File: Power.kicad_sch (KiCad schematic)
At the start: 57 parts, among them J6 Conn_01x02, Q3 AON7534, Q4 AON7534, U10 MAX17320G22+, U5 TPS259474ARPWR, U6 TPS2116DRL, U7 TPS61033DRLR, U9 BQ25798

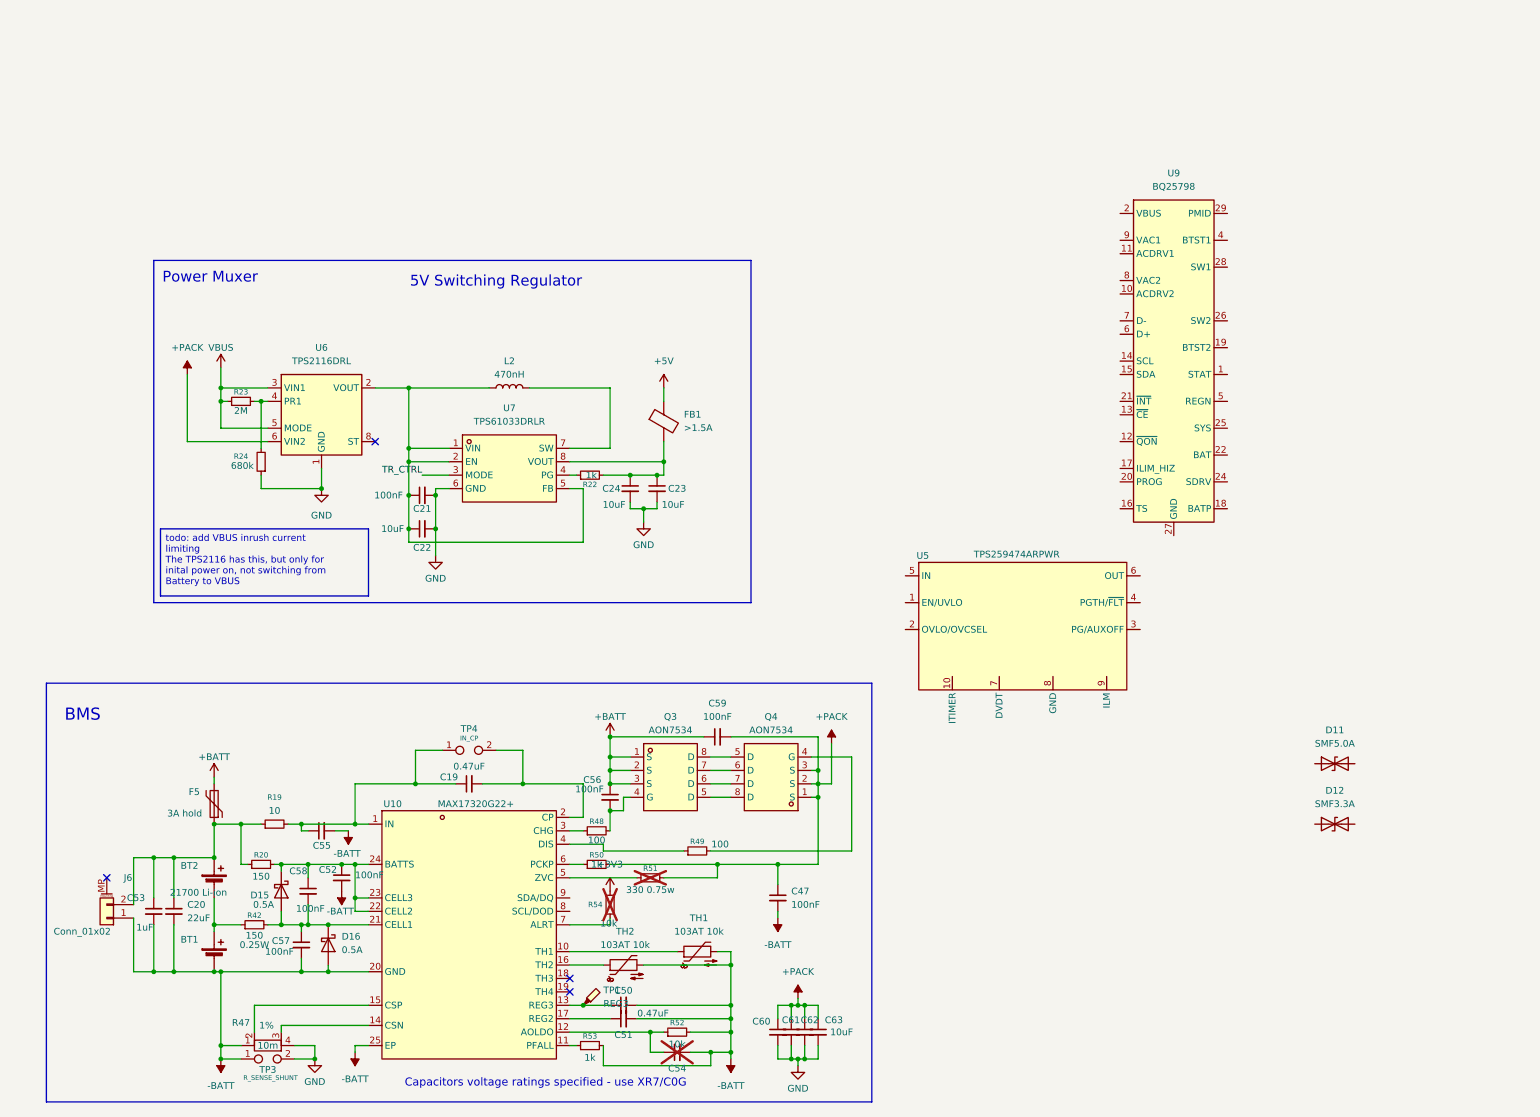
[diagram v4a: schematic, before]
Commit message: wired BQ25798 schematic
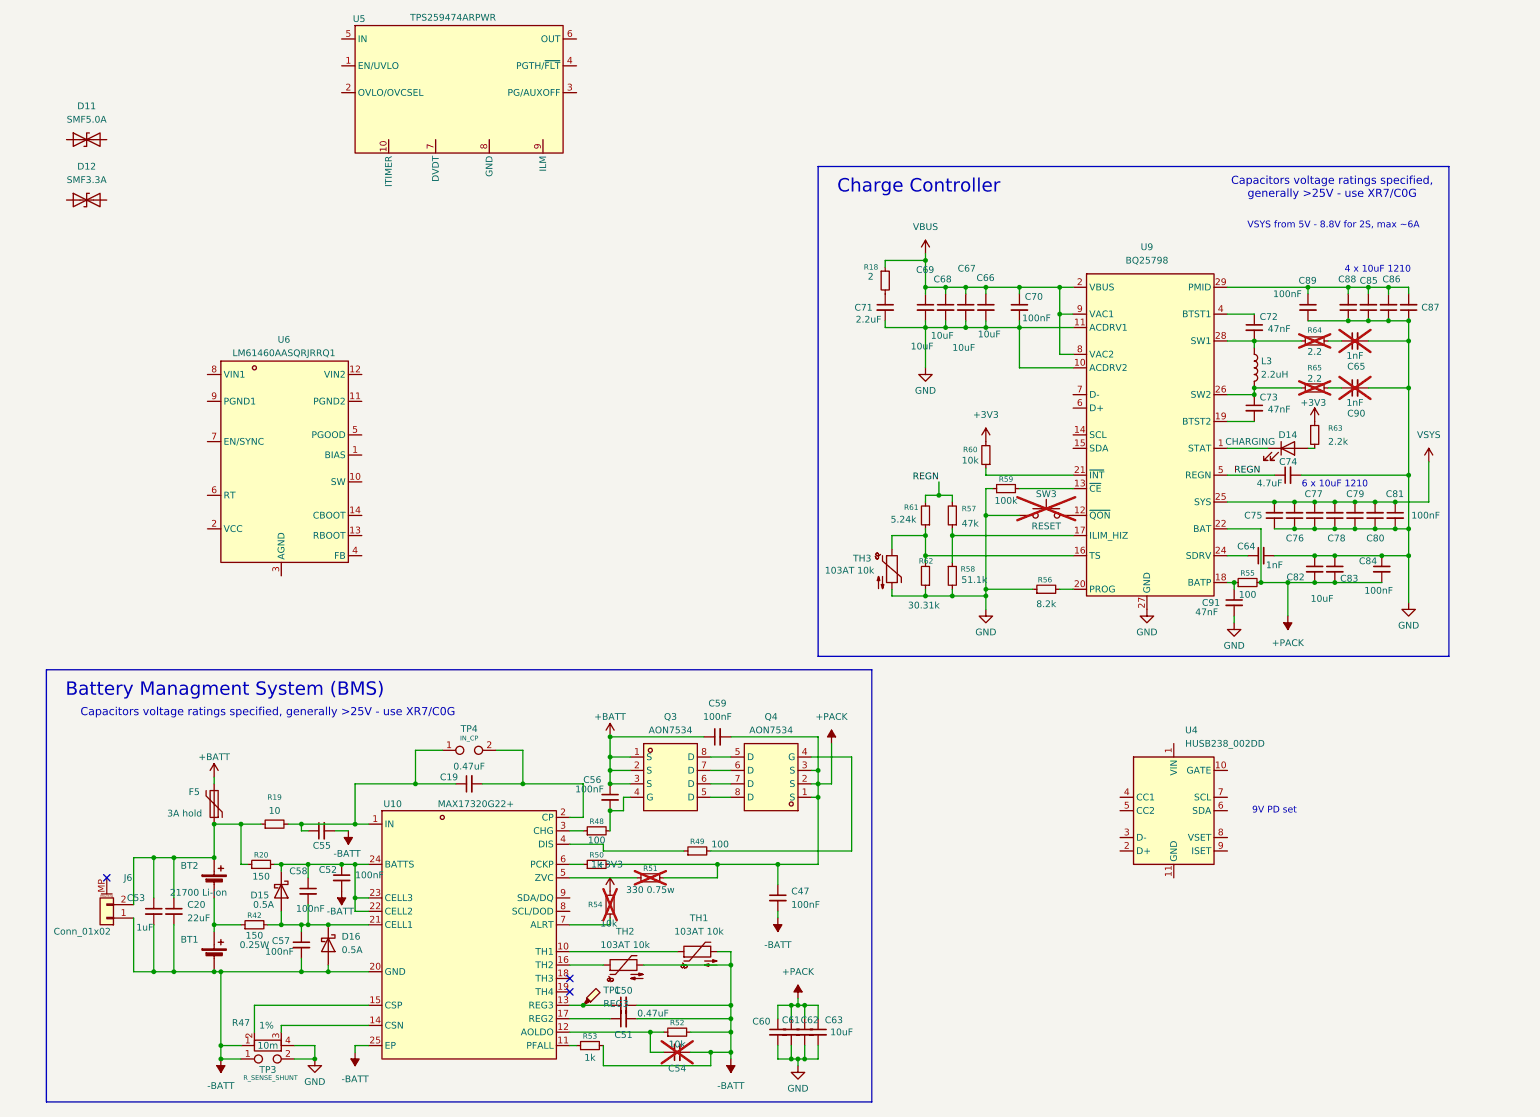
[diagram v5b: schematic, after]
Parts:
- removed C21: 100nF, Capacitor_SMD:C_0402_1005Metric, symbol Device:C_Small
- removed C22, C23, C24: 10uF, Capacitor_SMD:C_0402_1005Metric, symbol Device:C_Small
- removed FB1: >1.5A, Inductor_SMD:L_0805_2012Metric_Pad1.05x1.20mm_HandSolder, symbol Device:FerriteBead
- removed L2: 470nH, Inductor_SMD:L_1008_2520Metric_Pad1.43x2.20mm_HandSolder, symbol Device:L
- removed R22: 1k, Resistor_SMD:R_0402_1005Metric, symbol Device:R_Small
- removed R23: 2M, Resistor_SMD:R_0402_1005Metric, symbol Device:R_Small
- removed R24: 680k, Resistor_SMD:R_0402_1005Metric, symbol Device:R_Small
- removed U6: TPS2116DRL, Package_TO_SOT_SMD:SOT-583-8, symbol Power_Management:TPS2116DRL
- removed U7: TPS61033DRLR, Package_TO_SOT_SMD:SOT-583-8, symbol easyeda2kicad:TPS61033DRLR
- added C64: 1nF, Capacitor_SMD:C_0402_1005Metric, symbol Device:C_Small
- added C65, C90: 1nF, Capacitor_SMD:C_0402_1005Metric_Pad0.74x0.62mm_HandSolder, symbol Device:C_Small
- added C66, C67, C68, C69, C75, C76, C77, C78, C79, C80, C82, C83, C85, C86, C87, C88: 10uF, Capacitor_SMD:C_1210_3225Metric, symbol Device:C_Small
- added C70, C81, C84, C89: 100nF, Capacitor_SMD:C_0402_1005Metric, symbol Device:C_Small
- added C71: 2.2uF, Capacitor_SMD:C_0805_2012Metric, symbol Device:C_Small
- added C72, C73, C91: 47nF, Capacitor_SMD:C_0402_1005Metric, symbol Device:C_Small
- added C74: 4.7uF, Capacitor_SMD:C_0603_1608Metric, symbol Device:C_Small
- added D14: CHARGING, symbol Device:LED
- added L3: 2.2uH, symbol Device:L
- added R18: 2, Resistor_SMD:R_0402_1005Metric, symbol Device:R_Small
- added R55: 100, Resistor_SMD:R_0402_1005Metric, symbol Device:R_Small
- added R56: 8.2k, Resistor_SMD:R_0402_1005Metric_Pad0.72x0.64mm_HandSolder, symbol Device:R_Small
- added R57: 47k, Resistor_SMD:R_0603_1608Metric_Pad0.98x0.95mm_HandSolder, symbol Device:R_Small
- added R58: 51.1k, Resistor_SMD:R_0603_1608Metric_Pad0.98x0.95mm_HandSolder, symbol Device:R_Small
- added R59: 100k, Resistor_SMD:R_0402_1005Metric, symbol Device:R_Small
- added R60: 10k, Resistor_SMD:R_0402_1005Metric, symbol Device:R_Small
- added R61: 5.24k, Resistor_SMD:R_0603_1608Metric_Pad0.98x0.95mm_HandSolder, symbol Device:R_Small
- added R62: 30.31k, Resistor_SMD:R_0603_1608Metric_Pad0.98x0.95mm_HandSolder, symbol Device:R_Small
- added R63: 2.2k, Resistor_SMD:R_0402_1005Metric_Pad0.72x0.64mm_HandSolder, symbol Device:R_Small
- added R64, R65: 2.2, Resistor_SMD:R_0402_1005Metric_Pad0.72x0.64mm_HandSolder, symbol Device:R_Small
- added SW3: RESET, symbol Switch:SW_Push
- added TH3: 103AT 10k, symbol Device:Thermistor_NTC
- added U4: HUSB238_002DD, Package_DFN_QFN:WDFN-10-1EP_3x3mm_P0.5mm_EP1.8x2.5mm, symbol Interface_USB:HUSB238_xxxDD
- added U6: LM61460AASQRJRRQ1, easyeda2kicad:VQFN-14-HR_L4.0-W3.5-TL_LM61460AASQRJRRQ1, symbol easyeda2kicad:LM61460AASQRJRRQ1
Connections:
- net +3V3: now also R60.2, R63.1
- net +PACK: now also U9.22 (BAT), U9.23 (BAT), C82.2, C83.2, C84.2, R55.2
- net GND: now also U9.10 (ACDRV2), U9.11 (ACDRV1), U9.27 (GND), C64.2, C65.2, C66.2, C67.2, C68.2, C69.2, C70.2, C71.2, C74.2, C75.1, C76.1, C77.1, C78.1, C79.1, C80.1, C81.2, C82.1, C83.1, C84.1, C85.1, C86.1, C87.1, C88.1, C89.2, C90.2, C91.2, R56.1, R58.2, R59.1, R62.1, SW3.1, TH3.2
- net VBUS: now also U9.2 (VBUS), U9.3 (VBUS), U9.8 (VAC2), U9.9 (VAC1), C66.1, C67.1, C68.1, C69.1, C70.1, R18.1
- net at U9.1 (STAT): now also D14.1 (K)
- net at U9.12 (~{QON}): now also SW3.2
- net at U9.13 (~{CE}): now also R59.2
- net at U9.16 (TS): now also R61.1, R62.2, TH3.1
- net at U9.17 (ILIM_HIZ): now also R57.1, R58.1
- net at U9.18 (BATP): now also C91.1, R55.1
- net at U9.19 (BTST2): now also C73.2
- net at U9.20 (PROG): now also R56.2
- net at U9.21 (~{INT}): now also R60.1
- net at U9.24 (SDRV): now also C64.1
- net VSYS: now reaches U9.25 (SYS)
- net VSYS: now also C75.2, C76.2, C77.2, C78.2, C79.2, C80.2, C81.1
- net at U9.26 (SW2): now also C73.1, L3.2, R65.1
- net at U9.28 (SW1): now also C72.2, L3.1, R64.1
- net at U9.29 (PMID): now also C85.2, C86.2, C87.2, C88.2, C89.1
- net at U9.4 (BTST1): now also C72.1
- net REGN: now reaches U9.5 (REGN)
- net REGN: now also C74.1, R57.2, R61.2
- new net: C71.1, R18.2
- new net: C90.1, R65.2
- new net: C65.1, R64.2
- new net: D14.2 (A), R63.2
- no-connect marks 4 -> 3
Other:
- note added: "4 x 10uF 1210"
- note added: "6 x 10uF 1210"
- note added: "9V PD set"
- note added: "Battery Managment System (BMS)"
- note added: "Capacitors voltage ratings specified, generally >25V - use XR7/C0G"
- note added: "Charge Controller"
- note added: "VSYS from 5V - 8.8V for 2S, max ~6A"
- note removed: "5V Switching Regulator"
- note removed: "BMS"
- note removed: "Capacitors voltage ratings specified - use XR7/C0G"
- note removed: "Power Muxer"
- moved on the sheet: D11, D12, U5, U9

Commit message: changes
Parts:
- added C100, C103, C97: 100nF, Capacitor_SMD:C_0402_1005Metric, symbol Device:C_Small
- added C101, C94, C95, C98, C99: 10uF, Capacitor_SMD:C_1210_3225Metric, symbol Device:C_Small
- added C102, C96: 1uF, Capacitor_SMD:C_0603_1608Metric, symbol Device:C_Small
- added C104, C105: 2.2uF, Capacitor_SMD:C_0603_1608Metric, symbol Device:C_Small
- added C106: 22pF C0G, Capacitor_SMD:C_0402_1005Metric_Pad0.74x0.62mm_HandSolder, symbol Device:C_Small
- added C107, C92: 1uF, Capacitor_SMD:C_0402_1005Metric, symbol Device:C_Small
- added C109, C110: 2.2uF, symbol Device:C_Small
- added C21, C23, C24: 22uF, Capacitor_SMD:C_1206_3216Metric, symbol Device:C_Small
- added C22: 1nF, Capacitor_SMD:C_0402_1005Metric_Pad0.74x0.62mm_HandSolder, symbol Device:C_Small
- added JP9: SolderJumper_3_Bridged12, Jumper:SolderJumper-3_P1.3mm_Bridged12_RoundedPad1.0x1.5mm_NumberLabels, symbol Jumper:SolderJumper_3_Bridged12
- added L2: 1.5uH, symbol Device:L
- added R22: 6.04k, Resistor_SMD:R_0402_1005Metric_Pad0.72x0.64mm_HandSolder, symbol Device:R_Small
- added R23: 100k, Resistor_SMD:R_0402_1005Metric, symbol Device:R_Small
- added R24: 24.3k, Resistor_SMD:R_0402_1005Metric_Pad0.72x0.64mm_HandSolder, symbol Device:R_Small
- added R66: 100, Resistor_SMD:R_0402_1005Metric_Pad0.72x0.64mm_HandSolder, symbol Device:R_Small
- added R67: 10, Resistor_SMD:R_0402_1005Metric, symbol Device:R_Small
- added R68, R71: 100k, symbol Device:R_Small
- added R69: 1k, Resistor_SMD:R_0402_1005Metric_Pad0.72x0.64mm_HandSolder, symbol Device:R_Small
- added R70: 402k, symbol Device:R_Small
- added R72: 2.2, Resistor_SMD:R_0402_1005Metric_Pad0.72x0.64mm_HandSolder, symbol Device:R_Small
- added TP5: 5V, TestPoint:TestPoint_2Pads_Pitch2.54mm_Drill0.8mm, symbol Connector:TestPoint_2Pole
- added TP6: VSYS, TestPoint:TestPoint_2Pads_Pitch2.54mm_Drill0.8mm, symbol Connector:TestPoint_2Pole
- added TP8: PGOOD, TestPoint:TestPoint_Loop_D2.54mm_Drill1.5mm_Beaded, symbol Connector:TestPoint_Probe
- added U12: AP2112K-3.3TRG1, Package_TO_SOT_SMD:SOT-23-5, symbol Regulator_Linear:AP2112K-3.3
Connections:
- net +3V3: now also C107.1, C110.1, R68.1, U12.5 (VOUT)
- net GND: now also U6.11 (PGND2), U6.3 (AGND), U6.9 (PGND1), C100.1, C101.2, C102.2, C104.2, C105.1, C107.2, C109.2, C110.2, C21.2, C22.2, C23.2, C24.1, C92.2, C94.1, C95.1, C96.1, C97.2, C98.2, C99.2, R22.1, R24.1, R71.2, TP5.1, TP6.2, U12.2 (GND)
- net VSYS: now also U6.12 (VIN2), U6.8 (VIN1), C100.2, C101.1, C102.1, C94.2, C95.2, C96.2, C97.1, C98.1, C99.1, R70.1, TP6.1
- net at U6.1 (BIAS): now also C105.2, R67.1
- net at U6.10 (SW): now also C103.1, L2.1, R72.1
- net at U6.13 (RBOOT): now also R66.2
- net at U6.14 (CBOOT): now also C103.2, R66.1
- net at U6.2 (VCC): now also C104.1
- net at U6.4 (FB): now also C106.2, R23.1, R24.2
- net PGOOD: now reaches U6.5 (PGOOD)
- net PGOOD: now also R68.2, TP8.1
- net at U6.6 (RT): now also R22.2
- net at U6.7 (EN/SYNC): now also JP9.1 (A)
- new net: C22.1, R72.2
- new net: C106.1, R69.2
- new net: JP9.2 (C), R70.2, R71.1
- new net +5V: C109.1, C21.1, C23.1, C24.2, C92.1, L2.2, R23.2, R67.2, R69.1, TP5.2, U12.1 (VIN), U12.3 (EN)
- new net EN_BUCK: JP9.3 (B)
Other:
- note added: "3 x 10uF 1210"
- note added: "Battery Management System (BMS)"
- note added: "VSYS from 7.1V - 8.8V for 2S, max ~6A"
- note removed: "Battery Managment System (BMS)"
- note removed: "VSYS from 5V - 8.8V for 2S, max ~6A"
- moved on the sheet: U4, U6
